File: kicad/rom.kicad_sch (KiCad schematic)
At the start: 28 parts, among them U1 28C512, U34 74HC74

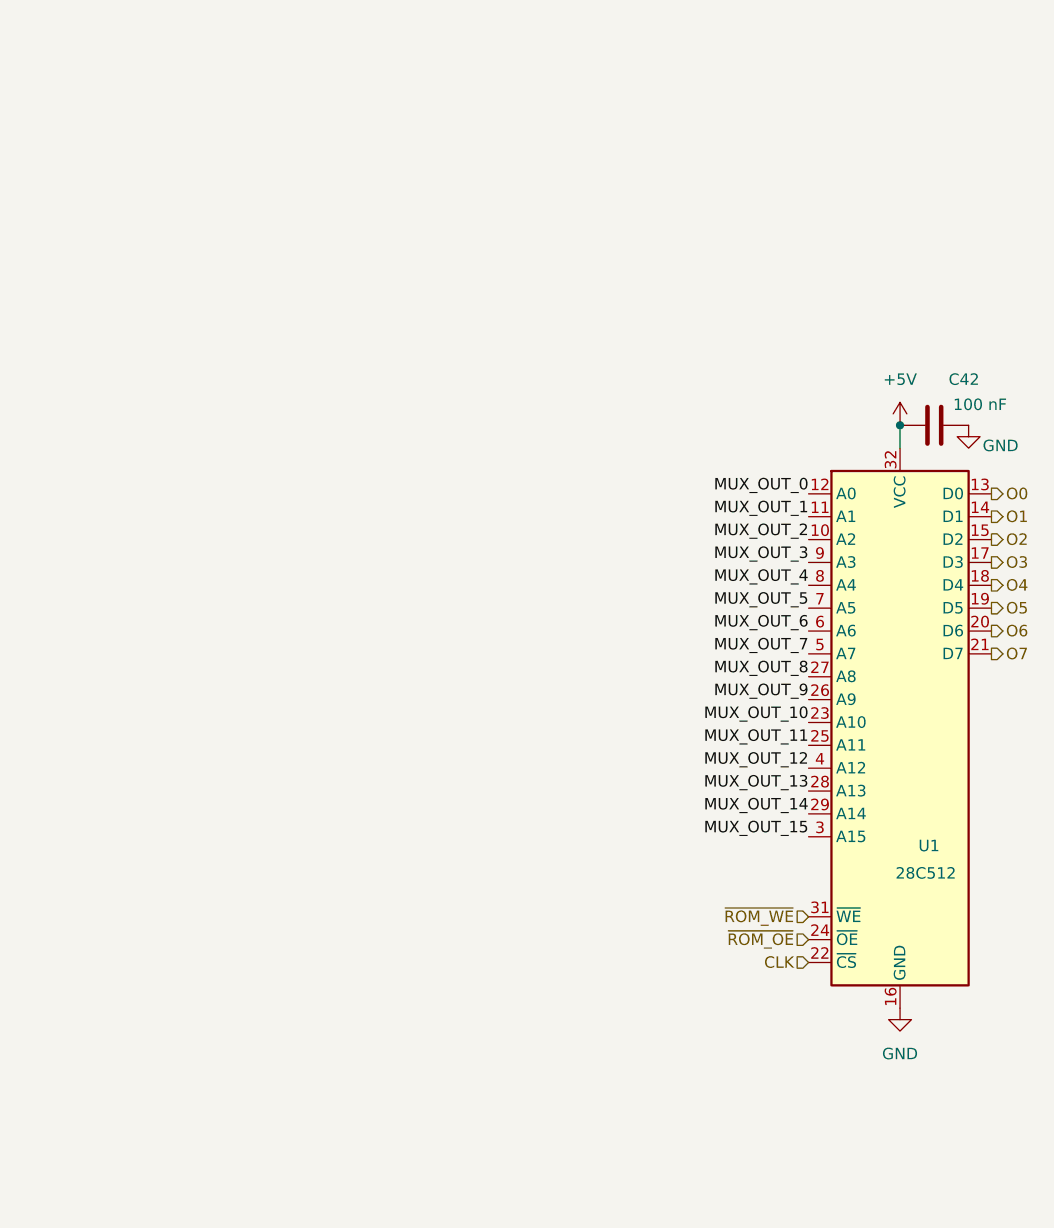
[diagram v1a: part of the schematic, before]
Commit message: kicad: compact design
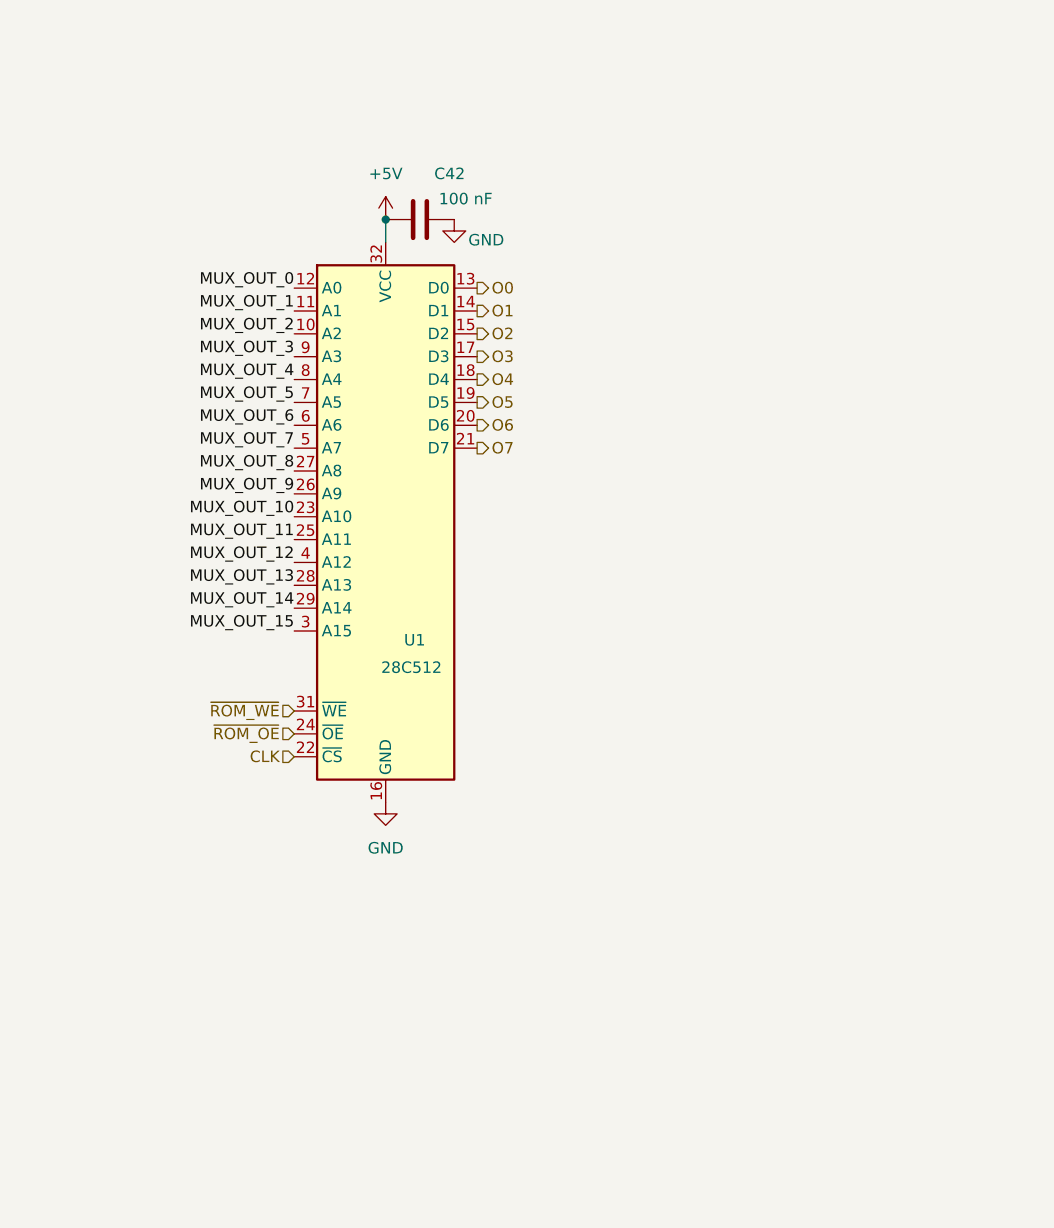
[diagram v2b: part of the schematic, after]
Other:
- moved on the sheet: C42, U1
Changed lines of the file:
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@@
 	)
 	(junction
-		(at 370.84 114.3)
+		(at 313.69 91.44)
 		(diameter 0)
 		(color 0 0 0 0)
@@
 	(wire
 		(pts
-			(xy 370.84 114.3) (xy 370.84 116.84)
+			(xy 313.69 91.44) (xy 313.69 93.98)
 		)
 		(stroke
@@
 	)
 	(label "MUX_OUT_14"
-		(at 360.68 157.48 180)
+		(at 303.53 134.62 180)
 		(effects
 			(font
@@
 	)
 	(label "MUX_OUT_2"
-		(at 360.68 127 180)
+		(at 303.53 104.14 180)
 		(effects
 			(font
@@
 	)
 	(label "MUX_OUT_0"
-		(at 360.68 121.92 180)
+		(at 303.53 99.06 180)
 		(effects
 			(font
@@
 	)
 	(label "MUX_OUT_1"
-		(at 360.68 124.46 180)
+		(at 303.53 101.6 180)
 		(effects
 			(font
@@
 	)
 	(label "MUX_OUT_11"
-		(at 360.68 149.86 180)
+		(at 303.53 127 180)
 		(effects
 			(font
@@
 	)
 	(label "MUX_OUT_9"
-		(at 360.68 144.78 180)
+		(at 303.53 121.92 180)
 		(effects
 			(font
@@
 	)
 	(label "MUX_OUT_3"
-		(at 360.68 129.54 180)
+		(at 303.53 106.68 180)
 		(effects
 			(font
@@
 	)
 	(label "MUX_OUT_4"
-		(at 360.68 132.08 180)
+		(at 303.53 109.22 180)
 		(effects
 			(font
@@
 	)
 	(label "MUX_OUT_7"
-		(at 360.68 139.7 180)
+		(at 303.53 116.84 180)
 		(effects
 			(font
@@
 	)
 	(label "MUX_OUT_10"
-		(at 360.68 147.32 180)
+		(at 303.53 124.46 180)
 		(effects
 			(font
@@
 	)
 	(label "MUX_OUT_5"
-		(at 360.68 134.62 180)
+		(at 303.53 111.76 180)
 		(effects
 			(font
@@
 	)
 	(label "MUX_OUT_15"
-		(at 360.68 160.02 180)
+		(at 303.53 137.16 180)
 		(effects
 			(font
@@
 	)
 	(label "MUX_OUT_8"
-		(at 360.68 142.24 180)
+		(at 303.53 119.38 180)
 		(effects
 			(font
@@
 	)
 	(label "MUX_OUT_13"
-		(at 360.68 154.94 180)
+		(at 303.53 132.08 180)
 		(effects
 			(font
@@
 	)
 	(label "MUX_OUT_12"
-		(at 360.68 152.4 180)
+		(at 303.53 129.54 180)
 		(effects
 			(font
@@
 	)
 	(label "MUX_OUT_6"
-		(at 360.68 137.16 180)
+		(at 303.53 114.3 180)
 		(effects
 			(font
@@
 	(hierarchical_label "O7"
 		(shape output)
-		(at 381 139.7 0)
+		(at 323.85 116.84 0)
 		(effects
 			(font
@@
 	(hierarchical_label "~{ROM_OE}"
 		(shape input)
-		(at 360.68 171.45 180)
+		(at 303.53 148.59 180)
 		(effects
 			(font
@@
 	(hierarchical_label "O4"
 		(shape output)
-		(at 381 132.08 0)
+		(at 323.85 109.22 0)
 		(effects
 			(font
@@
 	(hierarchical_label "O2"
 		(shape output)
-		(at 381 127 0)
+		(at 323.85 104.14 0)
 		(effects
 			(font
@@
 	(hierarchical_label "O0"
 		(shape output)
-		(at 381 121.92 0)
+		(at 323.85 99.06 0)
 		(effects
 			(font
@@
 	(hierarchical_label "CLK"
 		(shape input)
-		(at 360.68 173.99 180)
+		(at 303.53 151.13 180)
 		(effects
 			(font
@@
 	(hierarchical_label "O3"
 		(shape output)
-		(at 381 129.54 0)
+		(at 323.85 106.68 0)
 		(effects
 			(font
@@
 	(hierarchical_label "O6"
 		(shape output)
-		(at 381 137.16 0)
+		(at 323.85 114.3 0)
 		(effects
 			(font
@@
 	(hierarchical_label "~{ROM_WE}"
 		(shape input)
-		(at 360.68 168.91 180)
+		(at 303.53 146.05 180)
 		(effects
 			(font
@@
 	(hierarchical_label "O5"
 		(shape output)
-		(at 381 134.62 0)
+		(at 323.85 111.76 0)
 		(effects
 			(font
@@
 	(hierarchical_label "O1"
 		(shape output)
-		(at 381 124.46 0)
+		(at 323.85 101.6 0)
 		(effects
 			(font
@@
 	(symbol
 		(lib_id "custom:28C512")
-		(at 370.84 144.78 0)
+		(at 313.69 121.92 0)
 		(unit 1)
 		(exclude_from_sim no)
@@
 		(dnp no)
 		(property "Reference" "U1"
-			(at 372.872 161.036 0)
+			(at 315.722 138.176 0)
 			(effects
 				(font
@@
 		)
 		(property "Value" "28C512"
-			(at 370.332 164.084 0)
+			(at 313.182 141.224 0)
 			(effects
 				(font
@@
 		)
 		(property "Footprint" ""
-			(at 370.84 144.78 0)
+			(at 313.69 121.92 0)
 			(effects
 				(font
@@
 		)
 		(property "Datasheet" "http://ww1.microchip.com/downloads/en/DeviceDoc/doc0006.pdf"
-			(at 370.84 144.78 0)
+			(at 313.69 121.92 0)
 			(effects
 				(font
@@
 		)
 		(property "Description" "Paged Parallel EEPROM 256Kb (32K x 8), DIP-28/SOIC-28"
-			(at 370.84 144.78 0)
+			(at 313.69 121.92 0)
 			(effects
 				(font
@@
 	(symbol
 		(lib_id "power:GND")
-		(at 370.84 179.07 0)
+		(at 313.69 156.21 0)
 		(unit 1)
 		(exclude_from_sim no)
@@
 		(fields_autoplaced yes)
 		(property "Reference" "#PWR06"
-			(at 370.84 185.42 0)
+			(at 313.69 162.56 0)
 			(effects
 				(font
@@
 		)
 		(property "Value" "GND"
-			(at 370.84 184.15 0)
+			(at 313.69 161.29 0)
 			(effects
 				(font
@@
 		)
 		(property "Footprint" ""
-			(at 370.84 179.07 0)
+			(at 313.69 156.21 0)
 			(effects
 				(font
@@
 		)
 		(property "Datasheet" ""
-			(at 370.84 179.07 0)
+			(at 313.69 156.21 0)
 			(effects
 				(font
@@
 		)
 		(property "Description" "Power symbol creates a global label with name \"GND\" , ground"
-			(at 370.84 179.07 0)
+			(at 313.69 156.21 0)
 			(effects
 				(font
@@
 	(symbol
 		(lib_id "power:+5V")
-		(at 370.84 114.3 0)
+		(at 313.69 91.44 0)
 		(unit 1)
 		(exclude_from_sim no)
@@
 		(fields_autoplaced yes)
 		(property "Reference" "#PWR05"
-			(at 370.84 118.11 0)
+			(at 313.69 95.25 0)
 			(effects
 				(font
@@
 		)
 		(property "Value" "+5V"
-			(at 370.84 109.22 0)
+			(at 313.69 86.36 0)
 			(effects
 				(font
@@
 		)
 		(property "Footprint" ""
-			(at 370.84 114.3 0)
+			(at 313.69 91.44 0)
 			(effects
 				(font
@@
 		)
 		(property "Datasheet" ""
-			(at 370.84 114.3 0)
+			(at 313.69 91.44 0)
 			(effects
 				(font
@@
 		)
 		(property "Description" "Power symbol creates a global label with name \"+5V\""
-			(at 370.84 114.3 0)
+			(at 313.69 91.44 0)
 			(effects
 				(font
@@
 	(symbol
 		(lib_id "power:GND")
-		(at 378.46 114.3 0)
+		(at 321.31 91.44 0)
 		(unit 1)
 		(exclude_from_sim no)
@@
 		(dnp no)
 		(property "Reference" "#PWR0180"
-			(at 378.46 120.65 0)
+			(at 321.31 97.79 0)
 			(effects
 				(font
@@
 		)
 		(property "Value" "GND"
-			(at 382.016 116.586 0)
+			(at 324.866 93.726 0)
 			(effects
 				(font
@@
 		)
 		(property "Footprint" ""
-			(at 378.46 114.3 0)
+			(at 321.31 91.44 0)
 			(effects
 				(font
@@
 		)
 		(property "Datasheet" ""
-			(at 378.46 114.3 0)
+			(at 321.31 91.44 0)
 			(effects
 				(font
@@
 		)
 		(property "Description" "Power symbol creates a global label with name \"GND\" , ground"
-			(at 378.46 114.3 0)
+			(at 321.31 91.44 0)
 			(effects
 				(font
@@
 	(symbol
 		(lib_id "Device:C")
-		(at 374.65 114.3 90)
+		(at 317.5 91.44 90)
 		(unit 1)
 		(exclude_from_sim no)
@@
 		(dnp no)
 		(property "Reference" "C42"
-			(at 377.952 109.22 90)
+			(at 320.802 86.36 90)
 			(effects
 				(font
@@
 		)
 		(property "Value" "100 nF"
-			(at 379.73 112.014 90)
+			(at 322.58 89.154 90)
 			(effects
 				(font
@@
 		)
 		(property "Footprint" ""
-			(at 378.46 113.3348 0)
+			(at 321.31 90.4748 0)
 			(effects
 				(font
@@
 		)
 		(property "Datasheet" "~"
-			(at 374.65 114.3 0)
+			(at 317.5 91.44 0)
 			(effects
 				(font
@@
 		)
 		(property "Description" "Unpolarized capacitor"
-			(at 374.65 114.3 0)
+			(at 317.5 91.44 0)
 			(effects
 				(font

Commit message: kicad: finalize sketch
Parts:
- ADR1_U0: renamed from U6; footprint (none) -> Package_DIP:DIP-16_W7.62mm
- ADR1_U0_C1: renamed from C41; footprint (none) -> Capacitor_THT:C_Disc_D3.0mm_W1.6mm_P2.50mm
- ADR1_U1: renamed from U7; footprint (none) -> Package_DIP:DIP-16_W7.62mm
- ADR1_U1_C1: renamed from C40; footprint (none) -> Capacitor_THT:C_Disc_D3.0mm_W1.6mm_P2.50mm
- ADR2_U0: renamed from U8; footprint (none) -> Package_DIP:DIP-16_W7.62mm
- ADR2_U0_C1: renamed from C39; footprint (none) -> Capacitor_THT:C_Disc_D3.0mm_W1.6mm_P2.50mm
- ADR2_U1: renamed from U9; footprint (none) -> Package_DIP:DIP-16_W7.62mm
- ADR2_U1_C1: renamed from C38; footprint (none) -> Capacitor_THT:C_Disc_D3.0mm_W1.6mm_P2.50mm
- PC_U0: renamed from U10; footprint (none) -> Package_DIP:DIP-16_W7.62mm
- PC_U0_C1: renamed from C50; footprint (none) -> Capacitor_THT:C_Disc_D3.0mm_W1.6mm_P2.50mm
- PC_U1: renamed from U11; footprint (none) -> Package_DIP:DIP-16_W7.62mm
- PC_U1_C1: renamed from C49; footprint (none) -> Capacitor_THT:C_Disc_D3.0mm_W1.6mm_P2.50mm
- PC_U2: renamed from U12; footprint (none) -> Package_DIP:DIP-16_W7.62mm
- PC_U2_C1: renamed from C48; footprint (none) -> Capacitor_THT:C_Disc_D3.0mm_W1.6mm_P2.50mm
- PC_U3: renamed from U13; footprint (none) -> Package_DIP:DIP-16_W7.62mm
- PC_U3_C1: renamed from C47; footprint (none) -> Capacitor_THT:C_Disc_D3.0mm_W1.6mm_P2.50mm
- ROMMUX_U0: renamed from U14; footprint (none) -> Package_DIP:DIP-16_W7.62mm
- ROMMUX_U0_C1: renamed from C43; footprint (none) -> Capacitor_THT:C_Disc_D3.0mm_W1.6mm_P2.50mm
- ROMMUX_U1: renamed from U15; footprint (none) -> Package_DIP:DIP-16_W7.62mm
- ROMMUX_U1_C1: renamed from C44; footprint (none) -> Capacitor_THT:C_Disc_D3.0mm_W1.6mm_P2.50mm
- ROMMUX_U2: renamed from U16; footprint (none) -> Package_DIP:DIP-16_W7.62mm
- ROMMUX_U2_C1: renamed from C45; footprint (none) -> Capacitor_THT:C_Disc_D3.0mm_W1.6mm_P2.50mm
- ROMMUX_U3: renamed from U33; footprint (none) -> Package_DIP:DIP-16_W7.62mm
- ROMMUX_U3_C1: renamed from C46; footprint (none) -> Capacitor_THT:C_Disc_D3.0mm_W1.6mm_P2.50mm
- ROM_U1: renamed from U1; footprint (none) -> Package_DIP:DIP-32_W15.24mm
- ROM_U_C1: renamed from C42; footprint (none) -> Capacitor_THT:C_Disc_D3.0mm_W1.6mm_P2.50mm
- SWT_U1: renamed from U34; footprint (none) -> Package_DIP:DIP-14_W7.62mm
- SWT_U_C1: renamed from C37; footprint (none) -> Capacitor_THT:C_Disc_D3.0mm_W1.6mm_P2.50mm
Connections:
- net +5V: no longer ADR1_U0.7 (CEP), ADR1_U0.9 (~{PE}), ADR1_U1.7 (CEP), ADR1_U1.9 (~{PE}), ADR2_U0.7 (CEP), ADR2_U0.9 (~{PE}), ADR2_U1.7 (CEP), ADR2_U1.9 (~{PE})
- net ADR0_OUT_0 renamed ADR1_OUT0
- net ADR1_OUT0: no longer ADR1_U0.14 (Q0)
- net ADR0_OUT_1 renamed ADR1_OUT1
- net ADR1_OUT1: no longer ADR1_U0.13 (Q1)
- net ADR0_OUT_2 renamed ADR1_OUT2
- net ADR1_OUT2: no longer ADR1_U0.12 (Q2)
- net ADR0_OUT_3 renamed ADR1_OUT3
- net ADR1_OUT3: no longer ADR1_U0.11 (Q3)
- net ADR0_OUT_4 renamed ADR1_OUT4
- net ADR1_OUT4: no longer ADR1_U1.14 (Q0)
- net ADR0_OUT_5 renamed ADR1_OUT5
- net ADR1_OUT5: no longer ADR1_U1.13 (Q1)
- net ADR0_OUT_6 renamed ADR1_OUT6
- net ADR1_OUT6: no longer ADR1_U1.12 (Q2)
- net ADR0_OUT_7 renamed ADR1_OUT7
- net ADR1_OUT7: no longer ADR1_U1.11 (Q3)
- net ADR1_OUT_0 renamed ADR2_OUT0
- net ADR2_OUT0: now also ADR1_U0.14 (Q0)
- net ADR1_OUT_1 renamed ADR2_OUT1
- net ADR2_OUT1: now also ADR1_U0.13 (Q1)
- net ADR1_OUT_2 renamed ADR2_OUT2
- net ADR2_OUT2: now also ADR1_U0.12 (Q2)
- net ADR1_OUT_3 renamed ADR2_OUT3
- net ADR2_OUT3: now also ADR1_U0.11 (Q3); no longer ADR2_U0.11 (Q3)
- net ADR1_OUT_4 renamed ADR2_OUT4
- net ADR2_OUT4: now also ADR1_U1.14 (Q0)
- net ADR1_OUT_5 renamed ADR2_OUT5
- net ADR2_OUT5: now also ADR1_U1.13 (Q1)
- net ADR1_OUT_6 renamed ADR2_OUT6
- net ADR2_OUT6: now also ADR1_U1.12 (Q2)
- net ADR1_OUT_7 renamed ADR2_OUT7
- net ADR2_OUT7: now also ADR1_U1.11 (Q3)
- net MUX_OUT_0 renamed MUX_OUT0
- net MUX_OUT_1 renamed MUX_OUT1
- net MUX_OUT_10 renamed MUX_OUT10
- net MUX_OUT_11 renamed MUX_OUT11
- net MUX_OUT_12 renamed MUX_OUT12
- net MUX_OUT_13 renamed MUX_OUT13
- net MUX_OUT_14 renamed MUX_OUT14
- net MUX_OUT_15 renamed MUX_OUT15
- net MUX_OUT_2 renamed MUX_OUT2
- net MUX_OUT_3 renamed MUX_OUT3
- net MUX_OUT_4 renamed MUX_OUT4
- net MUX_OUT_5 renamed MUX_OUT5
- net MUX_OUT_6 renamed MUX_OUT6
- net MUX_OUT_7 renamed MUX_OUT7
- net MUX_OUT_8 renamed MUX_OUT8
- net MUX_OUT_9 renamed MUX_OUT9
- net PC_OUT_0 renamed PC_OUT0
- net PC_OUT_1 renamed PC_OUT1
- net PC_OUT_10 renamed PC_OUT10
- net PC_OUT_11 renamed PC_OUT11
- net PC_OUT_12 renamed PC_OUT12
- net PC_OUT_13 renamed PC_OUT13
- net PC_OUT_14 renamed PC_OUT14
- net PC_OUT_15 renamed PC_OUT15
- net PC_OUT_2 renamed PC_OUT2
- net PC_OUT_3 renamed PC_OUT3
- net PC_OUT_4 renamed PC_OUT4
- net PC_OUT_5 renamed PC_OUT5
- net PC_OUT_6 renamed PC_OUT6
- net PC_OUT_7 renamed PC_OUT7
- net PC_OUT_8 renamed PC_OUT8
- net PC_OUT_9 renamed PC_OUT9
- new net ADR12_I: ADR1_U0.7 (CEP), ADR1_U1.7 (CEP), ADR2_U0.7 (CEP), ADR2_U1.7 (CEP)
- new net ADR3_OUT3: ADR2_U0.11 (Q3)
- new net ~{ADR1_WE}: ADR1_U0.9 (~{PE}), ADR1_U1.9 (~{PE})
- new net ~{ADR2_WE}: ADR2_U0.9 (~{PE}), ADR2_U1.9 (~{PE})
- no-connect marks 0 -> 9
